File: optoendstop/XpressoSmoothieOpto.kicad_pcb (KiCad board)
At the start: 2 copper layers, 99.7 x 99.7 mm, 13 parts, among them IC1 TCST1103, IC11 TCST1103, J1 HEADER_4, M2 LOGO_OSHW, Q1 BS108D

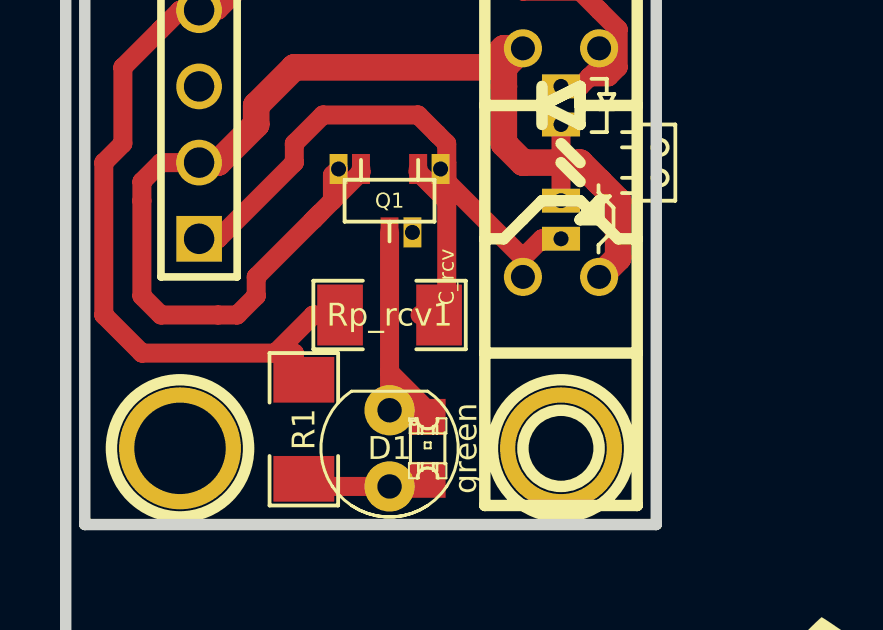
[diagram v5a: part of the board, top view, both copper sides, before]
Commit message: oe_clearance
optoendstops clearance check
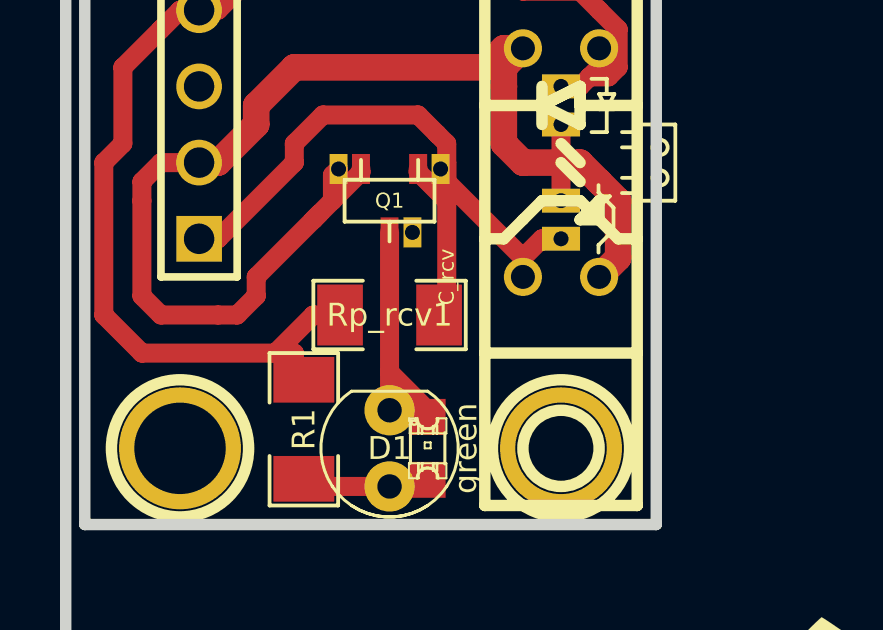
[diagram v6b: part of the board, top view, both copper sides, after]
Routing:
- net Signal1: track 25.2 -> 24.3 mm
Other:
- net class Default: clearance 0.2 -> 0.4
- rule trace_clearance: 0.2 -> 0.4
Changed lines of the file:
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@@
     (thickness 1.6)
     (drawings 14)
-    (tracks 92)
+    (tracks 91)
     (zones 0)
     (modules 13)
@@
     (user_trace_width 3)
     (user_trace_width 3.81)
-    (trace_clearance 0.2)
+    (trace_clearance 0.4)
     (zone_clearance 0.635)
     (zone_45_only yes)
@@
   (net 6 Signal1)
   (net_class Default "This is the default net class."
-    (clearance 0.2)
+    (clearance 0.4)
     (trace_width 0.635)
     (via_dia 1.27)
@@
   (segment (start 86.995 69.85) (end 84.455 67.31) (width 0.635) (layer F.Cu) (net 6))
   (segment (start 84.455 67.31) (end 84.455 66.675) (width 0.635) (layer F.Cu) (net 6))
-  (segment (start 83.566 71.755) (end 84.455 71.755) (width 0.635) (layer F.Cu) (net 6))
   (segment (start 76.835 69.215) (end 79.375 66.675) (width 0.635) (layer F.Cu) (net 6))
   (segment (start 79.375 66.675) (end 79.375 66.04) (width 0.635) (layer F.Cu) (net 6))

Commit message: oe
oe
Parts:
- moved RL_diode1 3.18 mm to (81.9, 60.3)
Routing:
- net 3.3V: track 29.7 -> 26.9 mm
- net N-000005: track 14.3 -> 11.9 mm
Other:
- board text added: "OSHW"
- board text removed: "x4"
- board text removed: "x5"
